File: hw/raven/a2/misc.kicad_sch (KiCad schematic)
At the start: 53 parts, among them J204 PinHdr_01x04, J401 DB25/9/9, J601 TRSx2, J606 DB9M/9M, J607 PS/2 (dual), U601 CNY17F-3, U602 74LS07

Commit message: Rev.A2 some minor fixes
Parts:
- JX607: Manufacturer_Name Preci-dip -> 3M; Manufacturer_Part_Number 540-88-068-24-008 -> 8468-11B1-RK-TP
- JX608: Manufacturer_Name Preci-dip -> 3M; Manufacturer_Part_Number 540-88-084-24-008 -> 8484-11B1-RK-TP
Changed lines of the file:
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@@
       (effects (font (size 1.27 1.27)))
     )
-    (property "Manufacturer_Name" "Preci-dip" (at 149.225 72.39 0)
-      (effects (font (size 1.27 1.27)) hide)
-    )
-    (property "Manufacturer_Part_Number" "540-88-084-24-008" (at 149.225 72.39 0)
+    (property "Manufacturer_Name" "3M" (at 149.225 72.39 0)
+      (effects (font (size 1.27 1.27)) hide)
+    )
+    (property "Manufacturer_Part_Number" "8484-11B1-RK-TP" (at 149.225 72.39 0)
       (effects (font (size 1.27 1.27)) hide)
     )
@@
       (effects (font (size 1.27 1.27)))
     )
-    (property "Manufacturer_Name" "Preci-dip" (at 128.905 72.39 0)
-      (effects (font (size 1.27 1.27)) hide)
-    )
-    (property "Manufacturer_Part_Number" "540-88-068-24-008" (at 128.905 72.39 0)
-      (effects (font (size 1.27 1.27)) hide)
-    )
+    (property "Manufacturer_Name" "3M" (at 128.905 72.39 0)
+      (effects (font (size 1.27 1.27)) hide)
+    )
+    (property "Manufacturer_Part_Number" "8468-11B1-RK-TP" (at 128.905 72.39 0)
+      (effects (font (size 1.27 1.27)) hide)
+    )

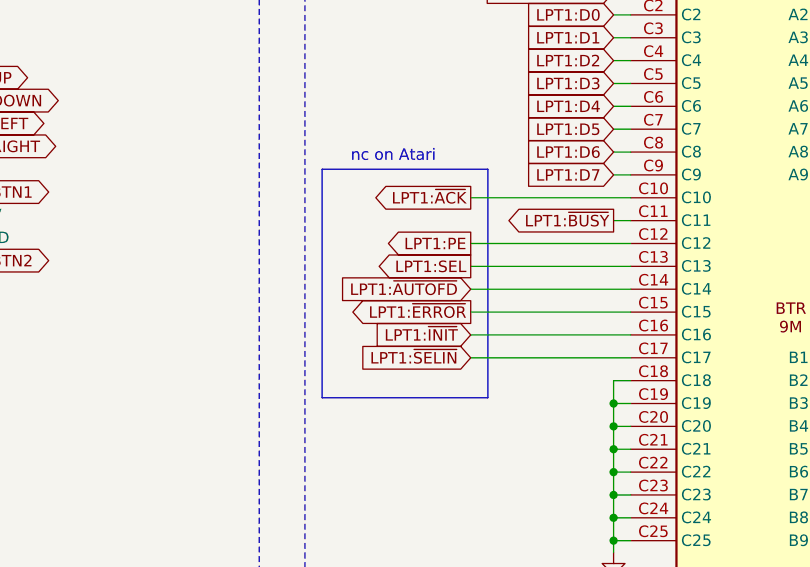
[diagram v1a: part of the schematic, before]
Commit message: rev.A2 updates
Added i2c DAC for reading cpu core temperature
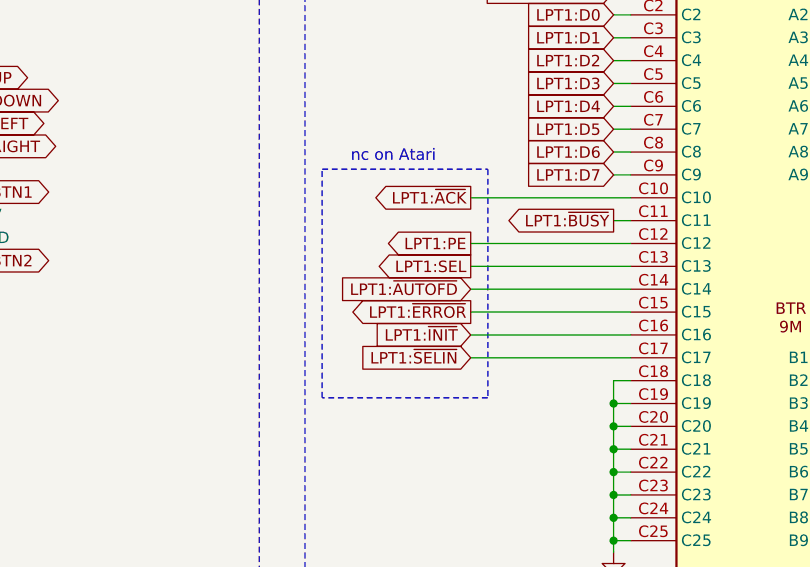
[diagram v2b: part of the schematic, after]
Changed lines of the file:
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@@
   )
   (rectangle (start 213.995 187.325) (end 232.41 212.725)
-    (stroke (width 0) (type default))
+    (stroke (width 0) (type dash))
     (fill (type none))
   )

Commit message: Raven.A2 wip
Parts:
- removed J607: PS/2 (dual), KMDGX6SGPS4N, symbol 68k:PS/2 (dual)
- added C605, C606, C608: 1u, Capacitor_SMD:C_1206_3216Metric_Pad1.33x1.80mm_HandSolder, symbol 68k:c_100nf_smd1206
- added C609: 0.1u, Capacitor_SMD:C_1206_3216Metric_Pad1.33x1.80mm_HandSolder, symbol 68k:c_100nf_smd1206
- added J607: USB+Ethernet, 68k:AMPHENOL_RJMG231022830ER, symbol 68k:RJMG231022830ER
- added J608: PinHdr_01x04, Connector_PinHeader_2.54mm:PinHeader_1x04_P2.54mm_Vertical, symbol Connector_Generic:Conn_01x04
- added NT601, NT602: NetTie_2, NetTie:NetTie-2_SMD_Pad0.5mm, symbol Device:NetTie_2
- added R612, R613: 470, Resistor_SMD:R_1206_3216Metric_Pad1.30x1.75mm_HandSolder, symbol Device:R
- gave numbers to parts that had none: 20
- renumbered C305 to C607, J204 to J602, J204 to J603, J204 to J604, J401 to J605
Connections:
- net +5V: now also C605.2, C606.2, J607.U11 (VCC_1), J607.U21 (VCC_2), J608.3 (Pin_3), R612.1, R613.1
- net GND: now also C605.1, C606.1, C608.1, C609.1, J607.1 (GND), J607.U14 (GND_1), J607.U24 (GND_2), J608.4 (Pin_4), NT601.1, NT602.1
- net SHIELD: now reaches J606.MH1
- net SHIELD: now also J605.MH1, J605.MH2, J605.MH3, J605.MH4, J606.MH2, J606.MH3, J606.MH4, J607.S1 (SHIELD_USB), J607.S2 (SHIELD_USB), J607.S3 (SHIELD_USB), J607.S4 (SHIELD_USB), J607.S5 (SHIELD), J607.S6 (SHIELD), J607.S7 (SHIELD), J607.S8 (SHIELD), NT601.2, NT602.2
- new net: J607.12, R612.2
- new net: J607.14, R613.2
- new net I2C_CLK: J608.1 (Pin_1)
- new net I2C_DTA: J608.2 (Pin_2)
- new net RJ:LED_GREEN: J607.13
- new net RJ:LED_YELLOW: J607.11
- new net RJ:TRD1+: J607.2 (TRD1+)
- new net RJ:TRD1-: J607.3 (TRD1-)
- new net RJ:TRD2+: J607.4 (TRD2+)
- new net RJ:TRD2-: J607.5 (TRD2-)
- new net RJ:VCC: C608.2, C609.2, J607.6 (VCC)
- new net USB1:D+: J607.U13 (D+_1)
- new net USB1:D-: J607.U12 (D-_1)
- new net USB2:D+: J607.U23 (D+_2)
- new net USB2:D-: J607.U22 (D-_2)
- no-connect marks 35 -> 32
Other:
- note added: "Adafruit STEMMA/Qwiic pinout"
- note added: "As close to pin as possible"
- note added: "Ethernet"
- note added: "I2C expansion header"
- note added: "RJ1"
- note added: "RJ2"
- note added: "RJ3"
- note added: "RJ4"
- note added: "RJ5"
- note added: "RJ6"
- note added: "RJ7"
- note added: "RJ8"
- note added: "USB Mouse + Keyboard"
- note added: "usb host"
- note added: "usb host / device"
- note removed: "PS2 Keyboard + Mouse"

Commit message: a2 wip
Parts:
- C605, C606: value 1u -> 10u; Manufacturer_Part_Number C1206C105K4RACTU -> C1206C106K4RAC
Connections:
- net +5V: no longer C605.2, C606.2, J607.U11 (VCC_1), J607.U21 (VCC_2)
- net USB1:D+ renamed USB0:D+
- net USB1:D- renamed USB0:D-
- new net VUSB: C605.2, C606.2, J607.U11 (VCC_1), J607.U21 (VCC_2)

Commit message: A2 rework
- reworking top-left area for dsp56303
- internal speaker header for YM
- software controlled volume for YM
- misc routing cleanup
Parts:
- removed C608: 1u, Capacitor_SMD:C_1206_3216Metric_Pad1.33x1.80mm_HandSolder, symbol 68k:c_100nf_smd1206
- removed C609: 0.1u, Capacitor_SMD:C_1206_3216Metric_Pad1.33x1.80mm_HandSolder, symbol 68k:c_100nf_smd1206
- removed NT602: NetTie_2, NetTie:NetTie-2_SMD_Pad0.5mm, symbol Device:NetTie_2
- removed R612, R613: 470, Resistor_SMD:R_1206_3216Metric_Pad1.30x1.75mm_HandSolder, symbol Device:R
- added C415, C416, C417, C418: 0.1u, Capacitor_SMD:C_1206_3216Metric_Pad1.33x1.80mm_HandSolder, symbol 68k:c_100nf_smd1206
- added C515: 10u, Capacitor_THT:CP_Radial_D5.0mm_P2.50mm, symbol Device:C_Polarized
- added J106: Pinhdr_01x02, Connector_PinHeader_2.54mm:PinHeader_1x02_P2.54mm_Vertical, symbol Connector_Generic:Conn_01x02
- added R332, R334, R340, R341, R342, R343: 10K, Resistor_SMD:R_1206_3216Metric_Pad1.30x1.75mm_HandSolder, symbol Device:R
- added U603: MCP4251, Package_SO:SOIC-14_3.9x8.7mm_P1.27mm, symbol Potentiometer_Digital:MCP4251-xxxx-SL
- added U604: PAM8302AAD, Package_SO:SOIC-8_3.9x4.9mm_P1.27mm, symbol Amplifier_Audio:PAM8302AAD
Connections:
- net +5V: now also C415.1, C417.2, C515.1, R341.1, R342.1, R343.1, U603.11 (~{WP}), U603.12 (~{SHDN}), U603.14 (VDD), U604.6 (VDD)
- net AUDIO_YM_L: now also R334.2, U603.9 (P0W); no longer R601.1, R602.1
- net AUDIO_YM_R: now also R332.2, U603.6 (P1W); no longer R603.1, R604.1
- net GND: now also C415.2, C417.1, C418.2, C515.2, R340.2, U603.10 (P0B), U603.4 (VSS), U603.5 (P1B), U604.7 (GND); no longer J607.1 (GND)
- net RJ:LED_GREEN: no longer names the net of J607.13
- net RJ:LED_YELLOW: no longer names the net of J607.11
- net RJ:TRD1+: no longer names the net of J607.2 (TRD1+)
- net RJ:TRD1-: no longer names the net of J607.3 (TRD1-)
- net RJ:TRD2+: no longer names the net of J607.4 (TRD2+)
- net RJ:TRD2-: no longer names the net of J607.5 (TRD2-)
- net RJ:VCC: no longer names the net of J607.6 (VCC)
- new net: C418.1, U604.4 (IN-)
- new net: C416.1, U604.3 (IN+)
- new net: C416.2, R332.1, R334.1
- new net: R601.1, R602.1, U603.8 (P0A)
- new net: R603.1, R604.1, U603.7 (P1A)
- new net AUDIO_SPK_M: J106.2 (Pin_2), U604.8 (OUT-)
- new net AUDIO_SPK_P: J106.1 (Pin_1), U604.5 (OUT+)
- new net YM:IOA0: R341.2, U603.1 (~{CS})
- new net YM:IOA1: R342.2, U603.2 (SCK)
- new net YM:IOA2: R343.2, U603.3 (SDI)
- new net YM:IOA6: R340.1, U604.1 (~{SD})
- no-connect marks 32 -> 28
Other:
- note added: "10kohm version"
- note added: "Internal speaker"
- note added: "cut1"
- note added: "cut2"
- note removed: "As close to pin as possible"
- note removed: "todo: header to route audio to/from ISA card"
- moved on the sheet: C601, C602, C603, C604, J601, J602, J603, J604, J608, R601, R602, R603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

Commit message: A2: DSP ram routing
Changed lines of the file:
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@@
 			(font
 				(size 2.54 2.54)
+				(thickness 0.508)
+				(bold yes)
 			)
 			(justify left bottom)
@@
 			(font
 				(size 2.54 2.54)
+				(thickness 0.508)
+				(bold yes)
 			)
 			(justify left bottom)
@@
 			(font
 				(size 1.27 1.27)
+				(thickness 0.254)
+				(bold yes)
 			)
 		)
@@
 			(font
 				(size 2.54 2.54)
+				(thickness 0.508)
+				(bold yes)
 			)
 			(justify left bottom)
@@
 			(font
 				(size 2.54 2.54)
+				(thickness 0.508)
+				(bold yes)
 			)
 			(justify left bottom)
@@
 			(font
 				(size 2.54 2.54)
+				(thickness 0.508)
+				(bold yes)
 			)
 			(justify left bottom)
@@
 			(font
 				(size 2.54 2.54)
+				(thickness 0.508)
+				(bold yes)
 			)
 			(justify left bottom)
@@
 			(font
 				(size 2.54 2.54)
+				(thickness 0.508)
+				(bold yes)
 			)
 			(justify left bottom)
@@
 			(font
 				(size 2.54 2.54)
+				(thickness 0.508)
+				(bold yes)
 			)
 			(justify left bottom)
@@
 			(font
 				(size 2.54 2.54)
-			)
-			(justify left bottom)
+				(thickness 0.508)
+				(bold yes)
+			)
+			(justify left bottom)

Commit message: a2, reannotate
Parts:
- renumbered C515 to C605, C415 to C606, C417 to C607, C416 to C608, C418 to C609, C605 to C610, C606 to C611, C607 to C612, J604 to J602, J602 to J603, J603 to J604, J106 to J605, J605 to J606, J608 to J607, J606 to J608, J607 to J609, R343 to R608, R342 to R609, R341 to R610, R332 to R611, R334 to R612, R340 to R613, R608 to R614, R609 to R615, R610 to R616, R611 to R617, U603 to U601, U604 to U602, U601 to U603, U602 to U604

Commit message: more a2 wip
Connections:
- net USB2:D+ renamed USB1:D+
- net USB2:D- renamed USB1:D-
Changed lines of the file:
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@@
 		)
 	)
-	(global_label "USB2:D-"
+	(global_label "USB1:D-"
 		(shape bidirectional)
 		(at 34.29 205.74 180)
@@
 		)
 	)
-	(global_label "USB2:D+"
+	(global_label "USB1:D+"
 		(shape bidirectional)
 		(at 34.29 208.28 180)
